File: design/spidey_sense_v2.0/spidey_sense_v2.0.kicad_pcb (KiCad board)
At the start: 2 copper layers, 46.7 x 51.3 mm, 37 parts, among them J1 Input_Screw_Terminal, J2 Output_Screw_Terminal, J3 Thermocouple_Terminal, J4 Thermocouple_Terminal, J5 Thermocouple_Terminal, J6 Thermocouple_Terminal, U1 LT1025, U2 LTC1983-5, U3 LT1001, U4 LT1001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

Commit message: Updated footprints
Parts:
- U1: footprint SamacSys_Parts:SOIC127P599X175-8N -> Package_SO:SOP-8_3.9x4.9mm_P1.27mm
- U2: footprint SamacSys_Parts:SOT95P280X100-6N -> Package_SO:TSOP-6_1.65x3.05mm_P0.95mm
- U3, U4, U5, U6: footprint SamacSys_Parts:NE555DR -> Package_SO:SOP-8_3.9x4.9mm_P1.27mm
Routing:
- net /Amplifier4/K+: track 48.0 -> 51.0 mm
- net -5V: track 59.5 -> 61.7 mm
- net GND: track 200.3 -> 198.9 mm

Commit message: Updated PCB
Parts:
- removed the REF** at (81.5, 65.8)
- removed the REF** at (116.3, 66.0)
- removed the REF** at (117.1, 85.1)
- removed the REF** at (81.5, 95.0)
- added REF**: MountingHole_3.2mm_M3_Pad, MountingHole:MountingHole_3.2mm_M3_Pad, F.Cu at (50.8, 66.6)
- added REF**: MountingHole_3.2mm_M3_Pad, MountingHole:MountingHole_3.2mm_M3_Pad, F.Cu at (105.8, 101.6)
- added REF**: MountingHole_3.2mm_M3_Pad, MountingHole:MountingHole_3.2mm_M3_Pad, F.Cu at (50.8, 101.6)
- added REF**: MountingHole_3.2mm_M3_Pad, MountingHole:MountingHole_3.2mm_M3_Pad, F.Cu at (105.8, 66.6)
- C10, C11, C8, C9, R6, R7, R8, R9, U5, U6: moved to F.Cu
- moved J3 66.7 mm to (58.2, 101.9), turned to 0 degrees
- moved J5 60.1 mm to (81.5, 101.9), turned to 0 degrees
- moved C4 43.3 mm to (54.6, 77.3)
- moved C1 43.2 mm to (67.7, 89.6), turned to 0 degrees
- moved C5 41.8 mm to (49.2, 82.0), turned to -90 degrees
- moved R4 37.2 mm to (67.6, 86.4), turned to 0 degrees
- moved C3 36.7 mm to (61.1, 81.9), turned to -90 degrees
- moved U2 36.6 mm to (54.4, 81.9), turned to -90 degrees
- moved C6 36.2 mm to (67.7, 80.5), turned to 0 degrees
- moved U3 33.7 mm to (76.1, 87.9)
- moved U4 33.1 mm to (76.1, 78.8)
- moved J4 32.4 mm to (69.8, 101.9)
- moved U1 31.1 mm to (51.6, 89.2), turned to 0 degrees
- moved R2 31.0 mm to (67.6, 77.2), turned to 0 degrees
- moved J1 29.0 mm to (85.1, 66.6), turned to 180 degrees
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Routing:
- net GND: track 198.9 -> 51.5 mm, vias 3 -> 9
- net +5V: track 112.3 -> 179.9 mm
- net -5V: track 61.7 -> 122.4 mm, vias 2 -> 0
- net /K-: track 136.2 -> 87.1 mm
- net /Amplifier4/Vout: track 37.0 -> 70.4 mm, vias 0 -> 1
- net /Amplifier1/Vout: track 51.0 -> 24.0 mm
- net /Amplifier4/K+: track 51.0 -> 24.2 mm, vias 0 -> 1
- net /Amplifier3/Vout: track 36.9 -> 60.9 mm, vias 0 -> 1
- net /Amplifier2/Vout: track 56.0 -> 35.3 mm, vias 2 -> 1
- net /Amplifier1/K+: track 23.8 -> 34.6 mm, vias 0 -> 1
- net /Amplifier3/K+: track 24.3 -> 34.6 mm, vias 0 -> 1
- net Net-(C7-Pad2): track 27.1 -> 34.4 mm
- net Net-(R1-Pad1): track 8.06 -> 14.1 mm
- net /Amplifier2/K+: track 28.5 -> 23.5 mm, vias 2 -> 1
- net Net-(C5-Pad1): track 3.22 -> 4.42 mm
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- added copper zone on B.Cu, net GND
- added copper zone on F.Cu, net GND
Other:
- board size 46.7 x 51.3 mm -> 63.5 x 46.5 mm
- board text added: "+5V"
- board text added: "GND"
- board text added: "K+"
- board text added: "K-"
- board text added: "Low ESR C4"
- board text added: "V3"
- board text added: "V4"
- board text added: "V5"
- board text added: "V6"

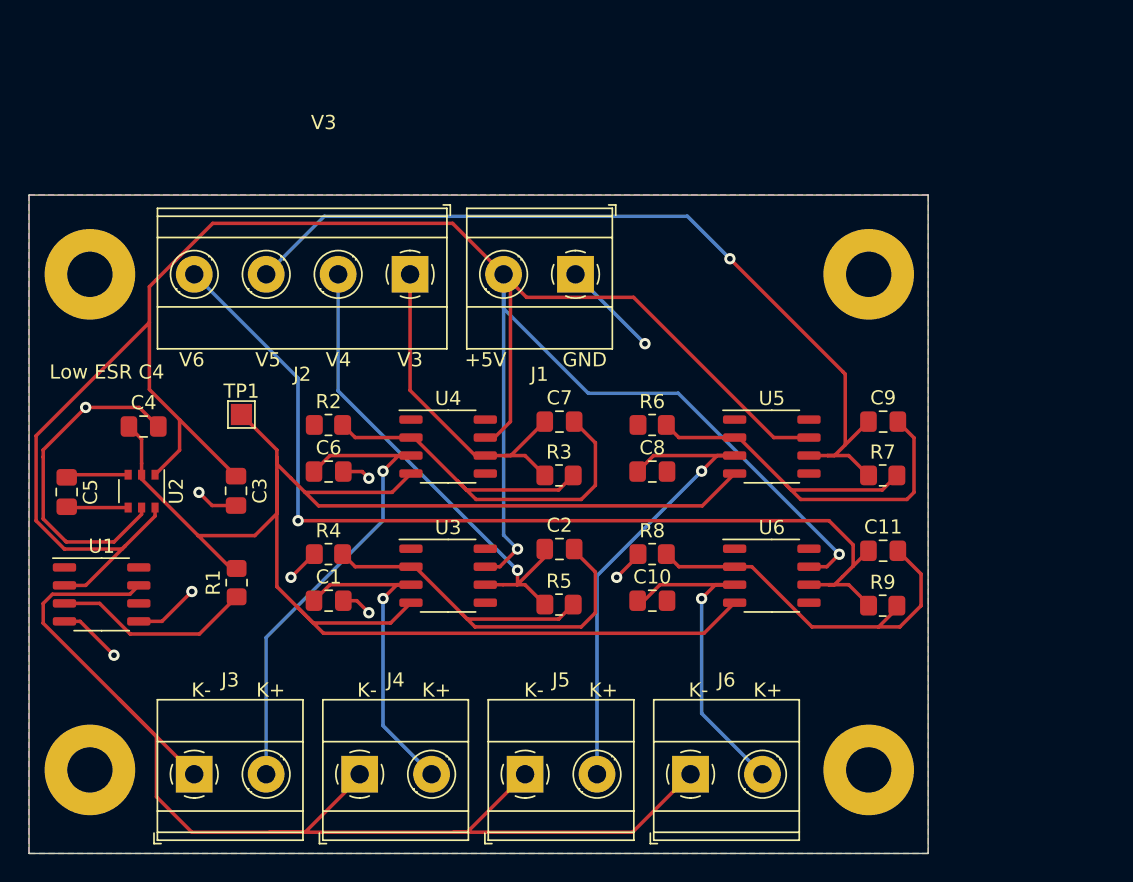
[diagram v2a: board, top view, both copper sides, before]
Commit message: Removed traces and daisy-chaining
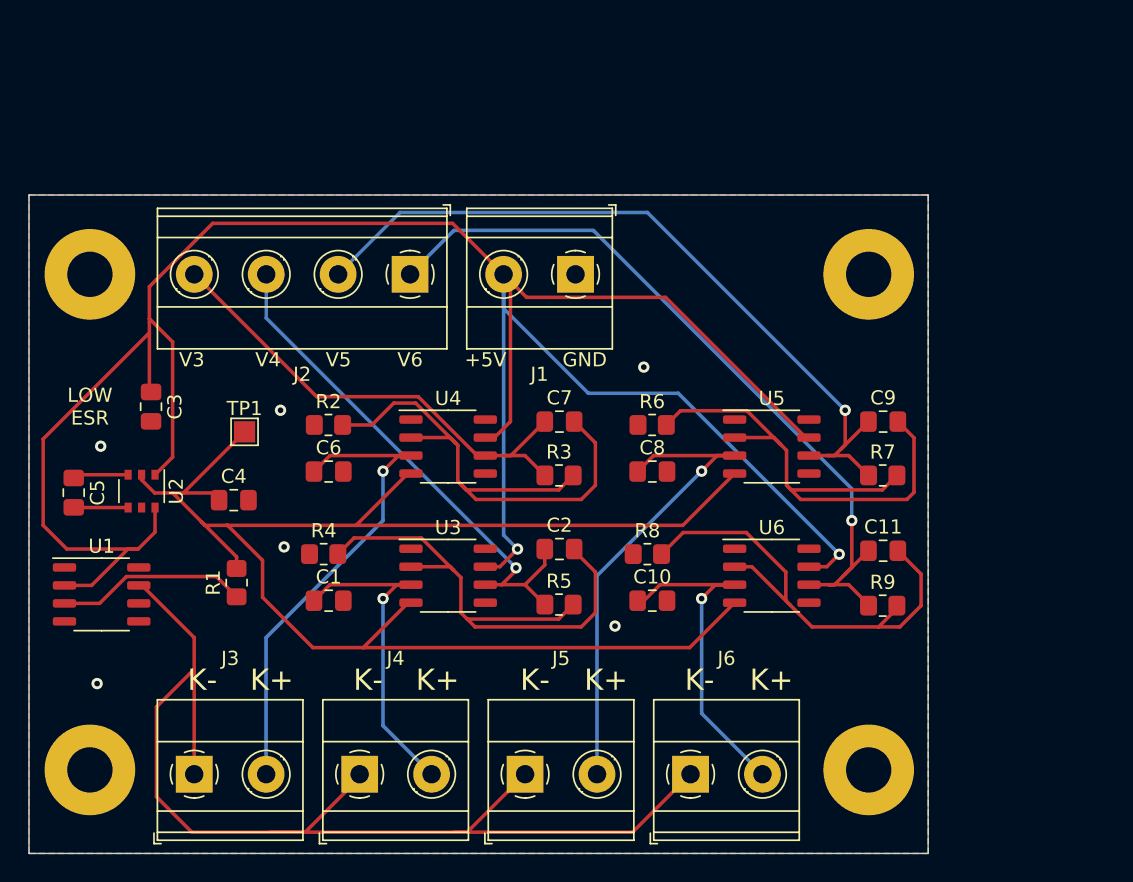
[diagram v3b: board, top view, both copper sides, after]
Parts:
- moved C3 8.45 mm to (55.1, 75.9)
- moved C4 8.22 mm to (61.0, 82.5)
- moved TP1 1.24 mm to (61.7, 77.7)
- moved C5 0.50 mm to (49.7, 82.0)
- moved R4 0.34 mm to (67.3, 86.4)
- moved R8 0.34 mm to (90.2, 86.4)
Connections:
- J2 pad 1: /Amplifier1/Vout -> /Amplifier4/Vout
- J2 pad 2: /Amplifier2/Vout -> /Amplifier3/Vout
- J2 pad 3: /Amplifier3/Vout -> /Amplifier2/Vout
- J2 pad 4: /Amplifier4/Vout -> /Amplifier1/Vout
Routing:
- net GND: track 51.5 -> 0.00 mm, vias 9 -> 6
- net /Amplifier4/Vout: track 70.4 -> 54.9 mm
- net -5V: track 122.4 -> 111.9 mm
- net /Amplifier1/Vout: track 24.0 -> 34.5 mm
- net Net-(C11-Pad2): track 27.3 -> 35.2 mm
- net /K-: track 87.1 -> 80.6 mm
- net Net-(C7-Pad2): track 34.4 -> 40.5 mm
- net /Amplifier3/Vout: track 60.9 -> 55.0 mm
- net Net-(C9-Pad2): track 33.7 -> 39.4 mm
- net Net-(C2-Pad2): track 34.1 -> 39.3 mm
- net /Amplifier2/Vout: track 35.3 -> 37.5 mm
- net +5V: track 179.9 -> 179.1 mm
- net Net-(R1-Pad1): track 14.1 -> 13.5 mm
- net Net-(C5-Pad2): track 4.36 -> 3.85 mm
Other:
- board text added: "LOW ESR"
- board text removed: "Low ESR C4"
